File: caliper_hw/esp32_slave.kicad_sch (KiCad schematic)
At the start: 3 parts, among them U1 ESP32_DevKit_V1_DOIT

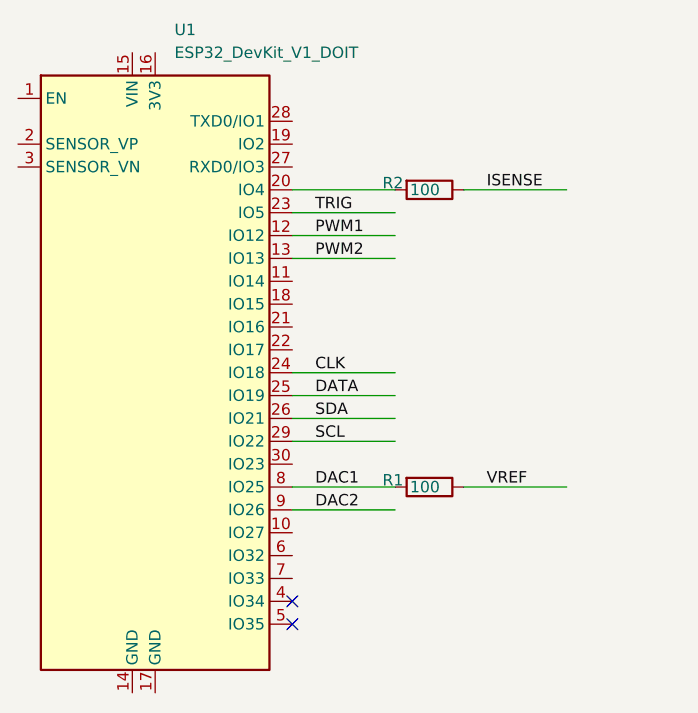
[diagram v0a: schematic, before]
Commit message: Update motor control system
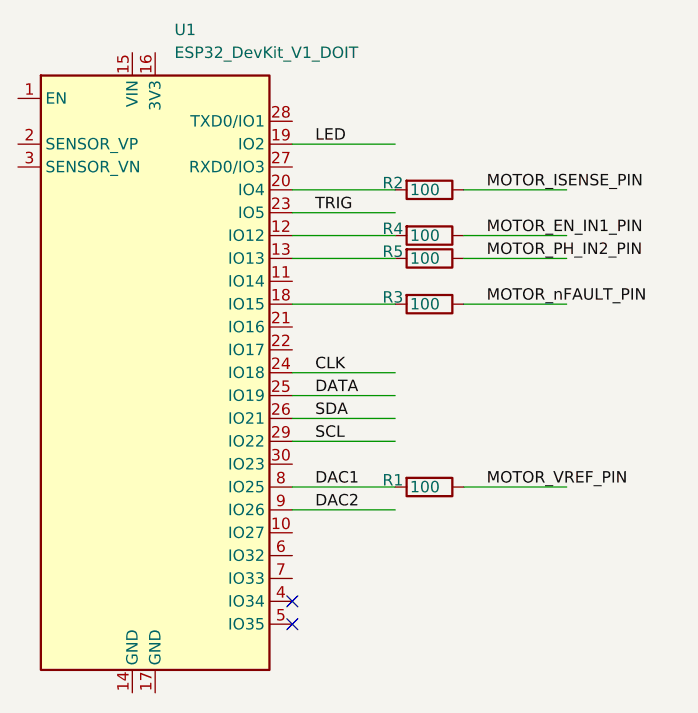
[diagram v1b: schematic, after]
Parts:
- added R3, R4, R5: 100, symbol Device:R
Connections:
- net at U1.18 (IO15): now also R3.2
- net LED: now reaches U1.19 (IO2)
- net ISENSE renamed MOTOR_ISENSE_PIN
- net PWM1: no longer names the net of U1.12 (IO12)
- net PWM1: now also R4.2
- net PWM2: no longer names the net of U1.13 (IO13)
- net PWM2: now also R5.2
- net VREF renamed MOTOR_VREF_PIN
- new net MOTOR_EN_IN1_PIN: R4.1
- new net MOTOR_PH_IN2_PIN: R5.1
- new net MOTOR_nFAULT_PIN: R3.1
